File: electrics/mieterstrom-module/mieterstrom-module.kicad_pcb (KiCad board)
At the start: 2 copper layers, 86 x 31 mm, 25 parts, among them J1 North, J2 South, J3 West, J4 East, U1 BA033CC0FP-E2, U2 MAX3486, U3 MAX3486

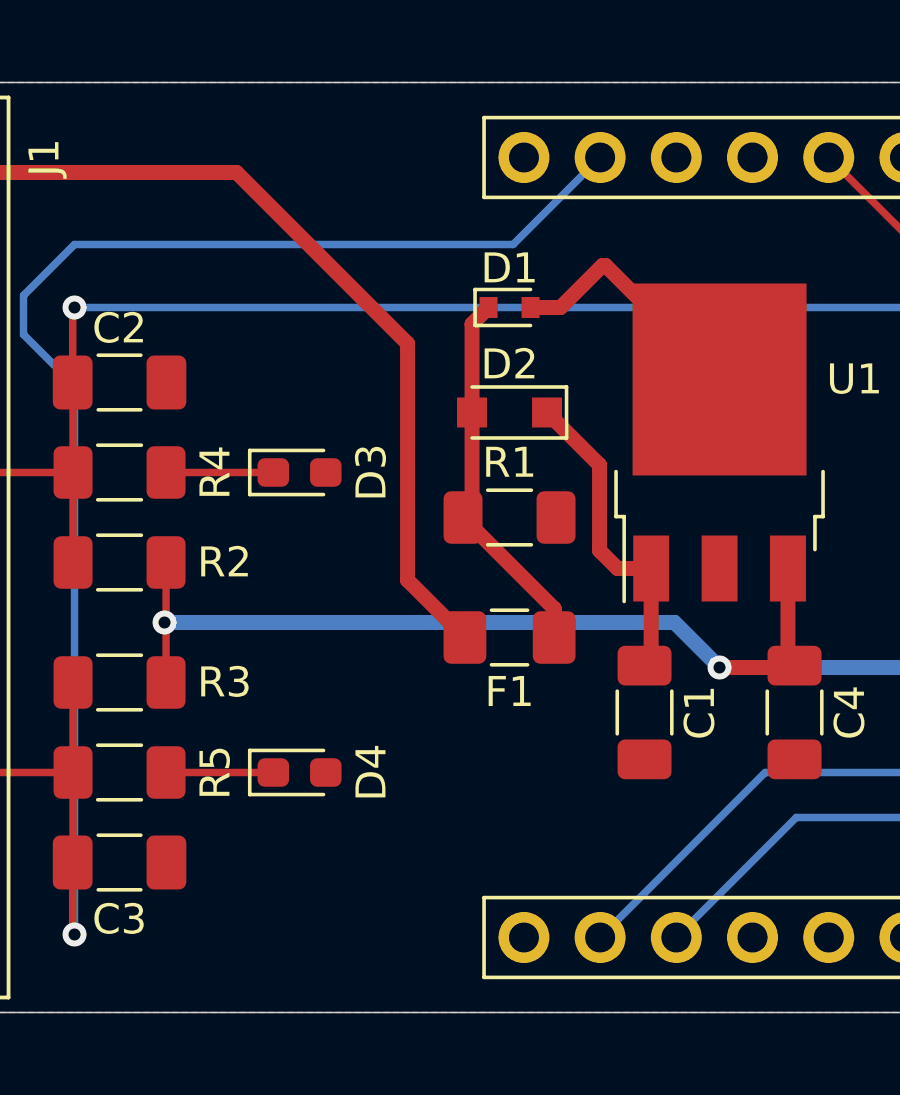
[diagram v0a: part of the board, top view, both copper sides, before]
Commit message: M bus module (#12)
* Fix wrong resistor manufacturer number in panel module

* Added missing labels for bus connectors in "Mieterstrom" module

* Added missing 3D model for BC66NB

* Finalized PoC for M-Bus module

* Updated documentation
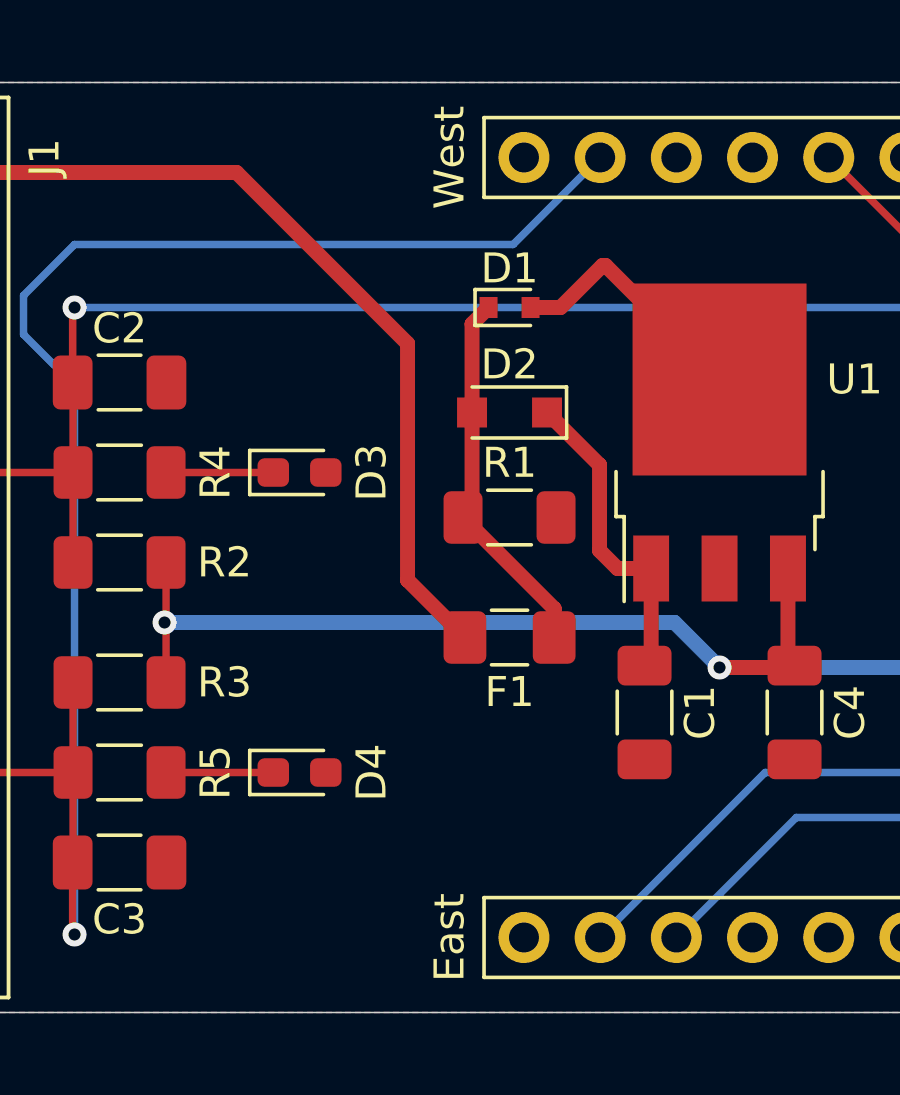
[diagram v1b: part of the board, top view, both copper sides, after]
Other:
- board text added: "East"
- board text added: "West"
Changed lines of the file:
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@@
     (effects (font (size 0.75 0.75) (thickness 0.1)))
+  )
+  (gr_text "West" (at 130 93.5 90) (layer "F.SilkS")
+    (effects (font (size 1 1) (thickness 0.15)))
   )
   (gr_text "GrayC GmbH" (at 156.5 107.5) (layer "F.SilkS")
     (effects (font (size 0.75 0.75) (thickness 0.1)))
   )
+  (gr_text "East" (at 130 119.5 90) (layer "F.SilkS")
+    (effects (font (size 1 1) (thickness 0.15)))
+  )
   (segment (start 133.25 102) (end 135 103.75) (width 0.5) (layer "F.Cu") (net 1))
